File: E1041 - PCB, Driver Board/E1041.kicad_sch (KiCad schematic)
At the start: 65 parts, among them J1 Barrel_Jack, J2 Screw_Terminal_01x02, J23 Conn_01x06_Female, J4 Conn_Coaxial, J5 Conn_01x03, J6 USB_C_Receptacle_USB2.0_14P, Q1 MMBT3904, U10 TPS61040DBV, U3 AP62200WU-7, U5 ESP32-PICO-D4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

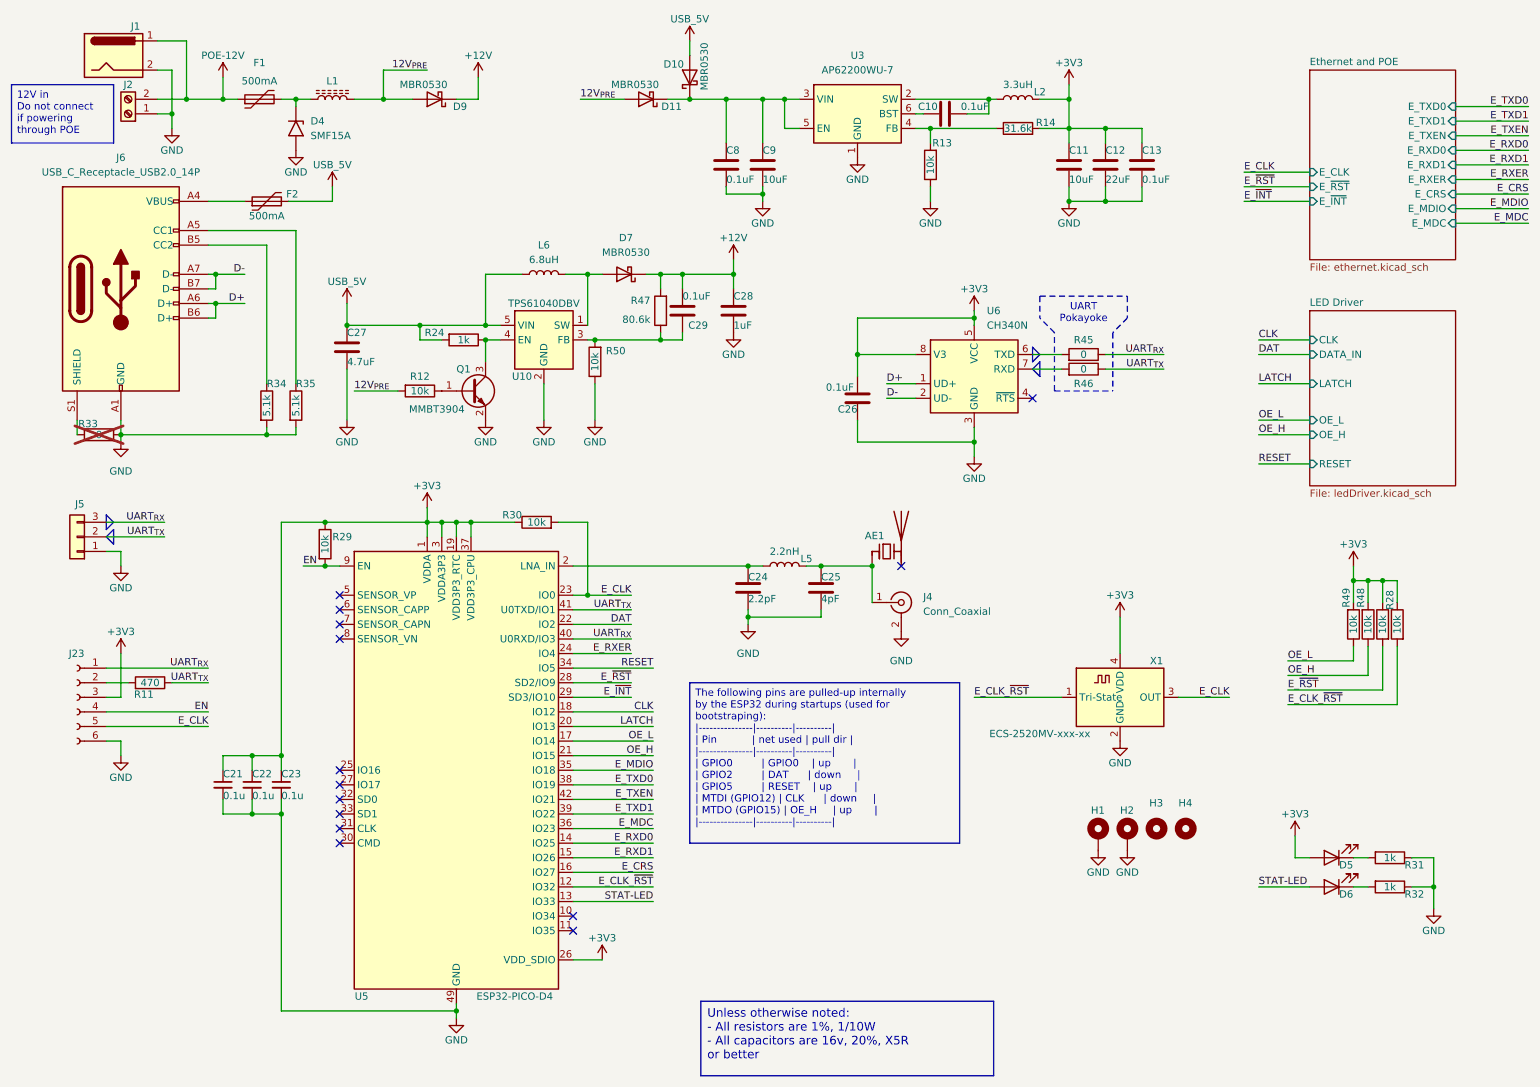
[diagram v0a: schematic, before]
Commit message: Added 'Part Number' in schematic, no design change
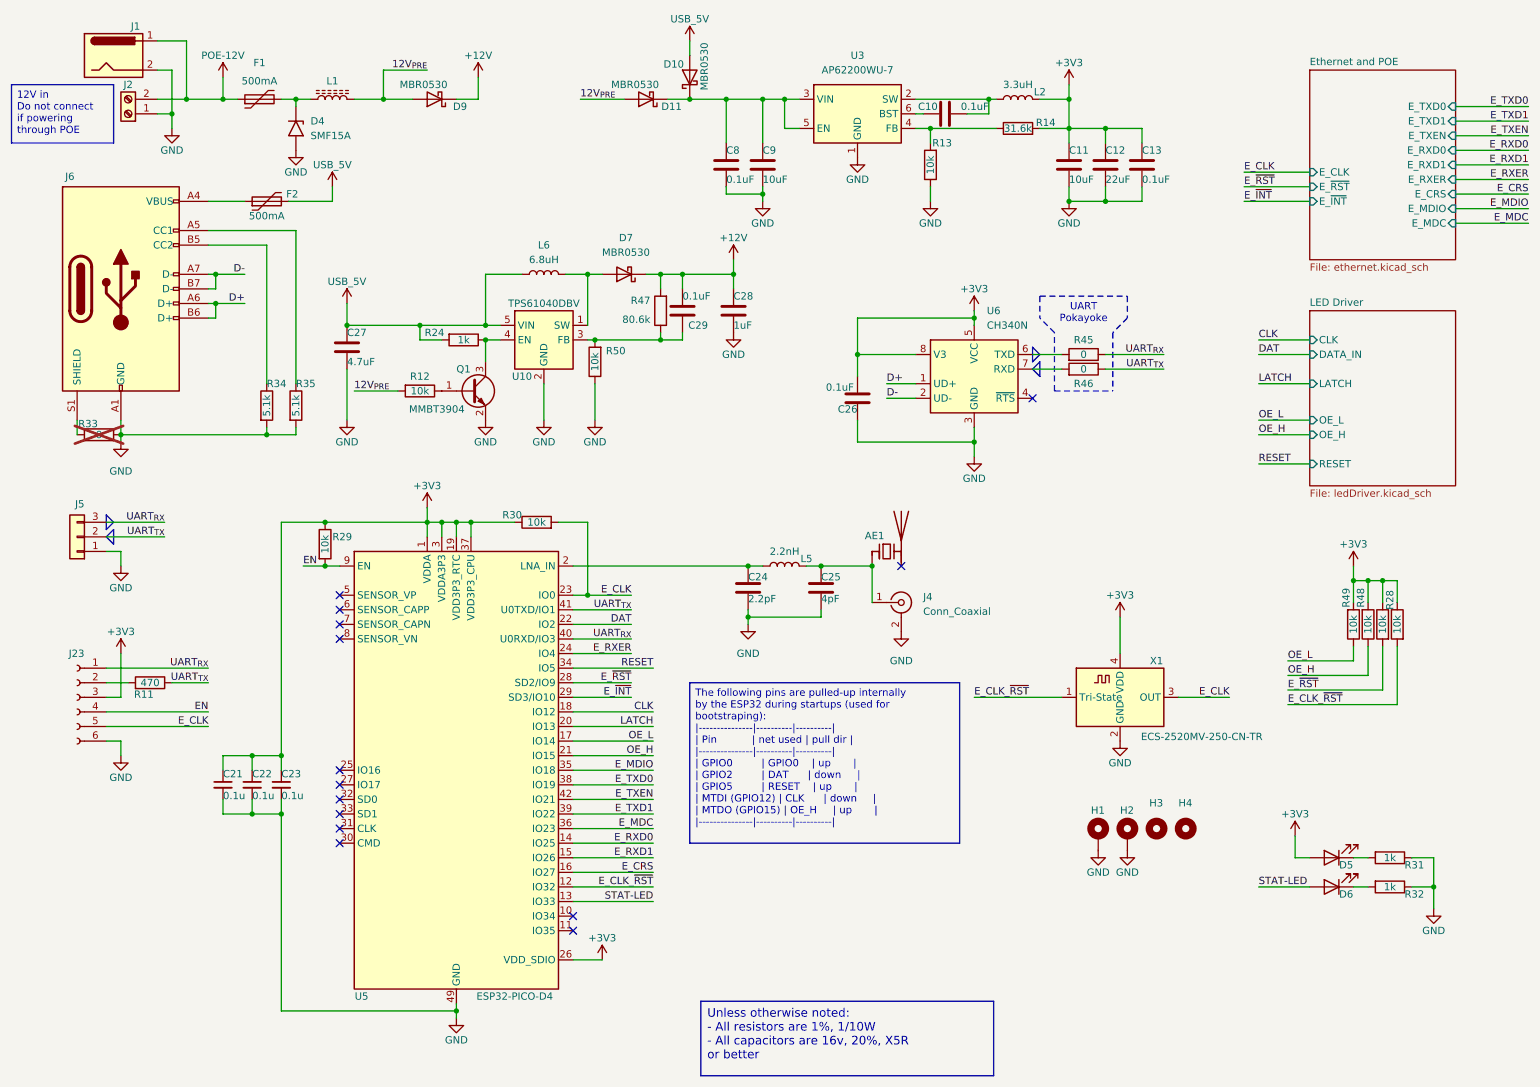
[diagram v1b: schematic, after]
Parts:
- AE1: Part Number (none) -> 2450AT43F0100001E
- D10, D11, D7, D9: Part Number (none) -> MBR0530
- D4: Part Number (none) -> SMF15A
- F1, F2: Part Number (none) -> 0ZCJ0050FF2G
- J1: Part Number (none) -> PJ-202A
- J2: Part Number (none) -> 1751248
- J6: Part Number (none) -> USB4105-GF-A
- L1: Part Number (none) -> BLM21AG102SN1D
- L2: Part Number (none) -> MAMK2520T3R3M
- L5: Part Number (none) -> L-14C2N2SV4T
- L6: Part Number (none) -> 1239AS-H-6R8M=P2
- Q1: Part Number (none) -> MMBT3904
- U10: Part Number (none) -> TPS61040DBV
- U3: Part Number (none) -> AP62200WU-7r
- U5: Part Number (none) -> ESP32-PICO-D4
- U6: Part Number (none) -> CH340N
- X1: value ECS-2520MV-xxx-xx -> ECS-2520MV-250-CN-TR; Part Number (none) -> ECS-2520MV-250-CN-TR
